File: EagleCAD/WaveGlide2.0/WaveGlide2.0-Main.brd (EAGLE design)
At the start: 80 x 100 mm, 47 parts, among them CN3 0, IC1 MC33502D, K2 MS-20-310-HN, Q2 reset, U1 ATMEGA328P_TQFP, U2 BMP180, U3 MPXV7002, U4 TPS55340PWP, U5 UG-2828GDEDF11, Y2 12MHz

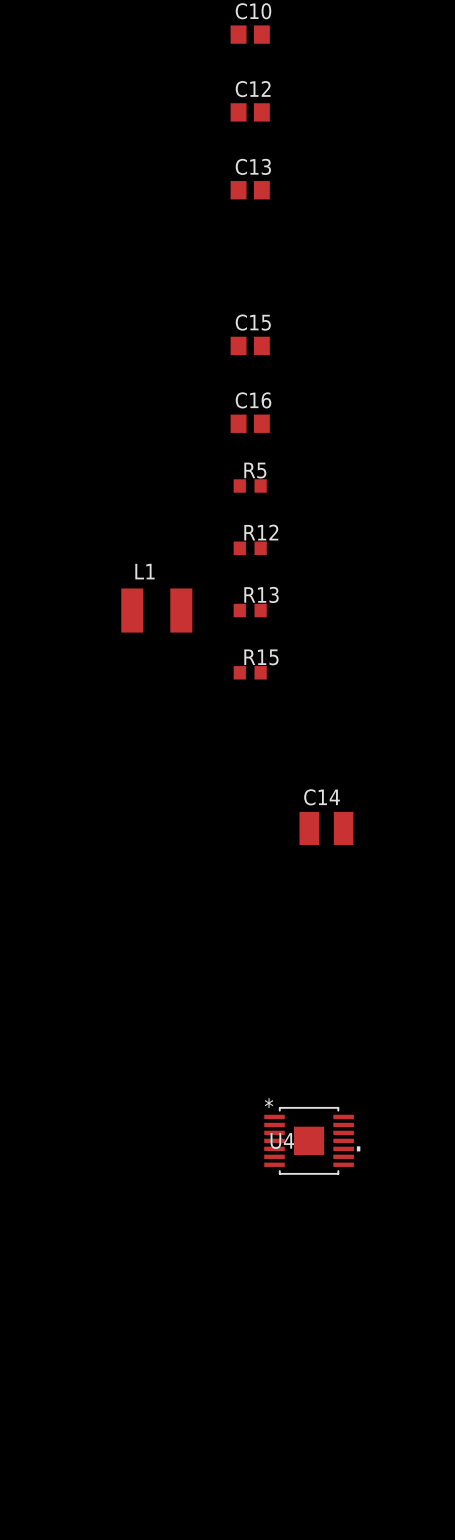
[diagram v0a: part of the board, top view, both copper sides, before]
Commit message: Add 5V regulator
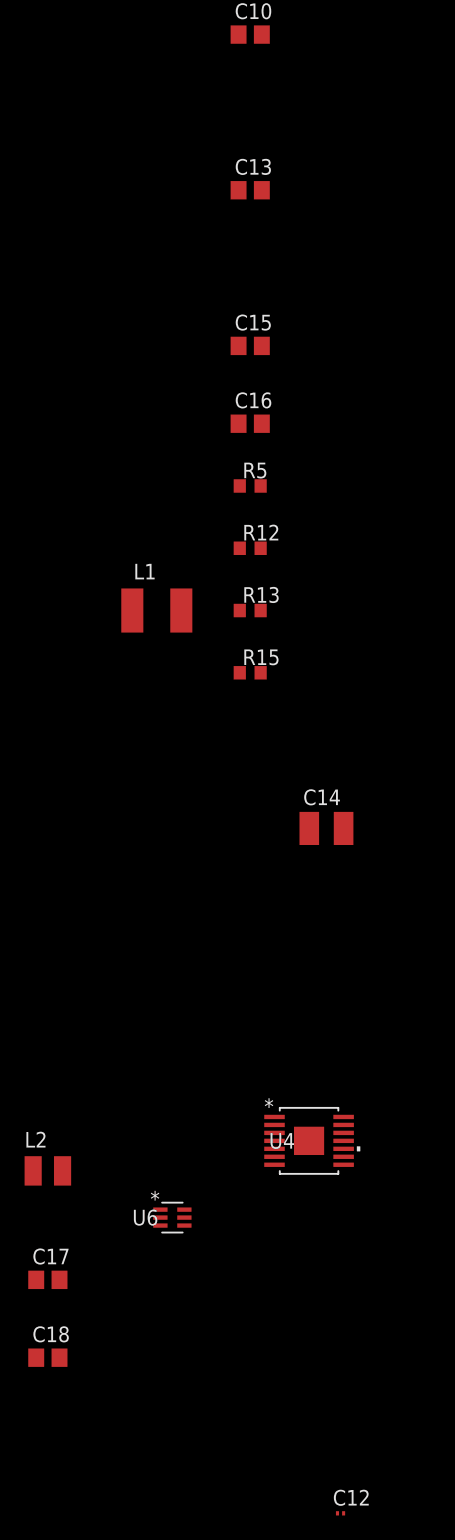
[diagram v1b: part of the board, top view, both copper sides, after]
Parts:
- added C17, C18: 10uF, resistor:C0805
- added L2: 4.7uH, resistor:L2825P
- added U6: TPS61222DCKR, CustomParts:DCK6
- C12: device resistor:C0805 -> resistor:C0201
- moved C12 114.5 mm to (-0.25, -132.1)
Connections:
- new net 5V_EN: U6.6
- new net N$6: L2.2, U6.5
- net GND: now also C17.2, C18.2, U6.3
- net SYS_5V: now also C18.1, U6.2, U6.4
- net TPS55340_SW: now also L1.2; no longer L1.1
- net VBAT: now also C17.1, L1.1, L2.1, U6.1; no longer L1.2

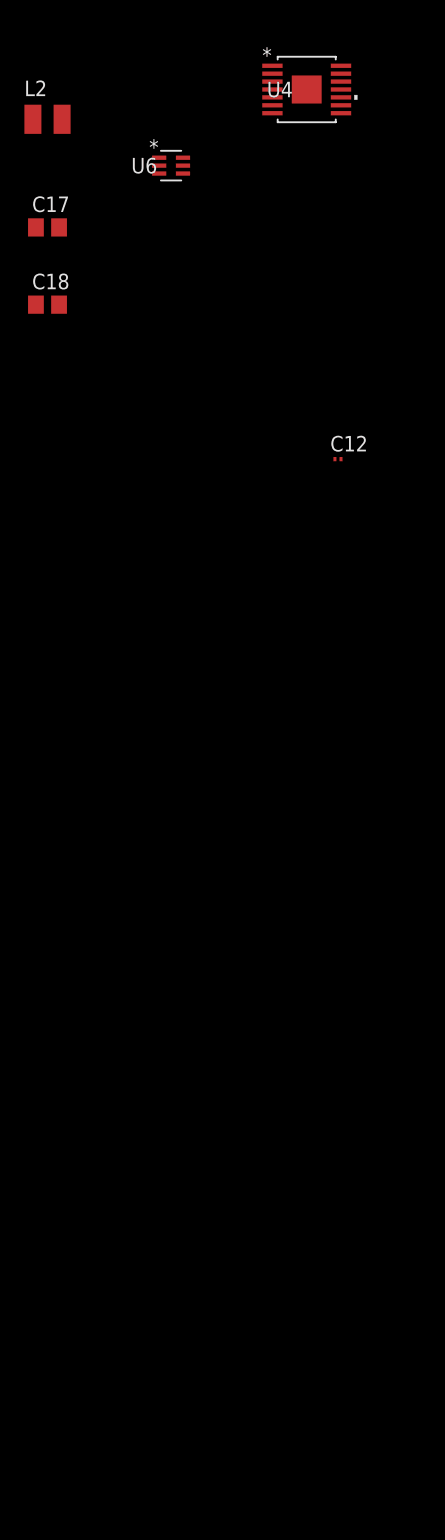
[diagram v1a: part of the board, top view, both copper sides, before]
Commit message: Add 13V boost for OLED
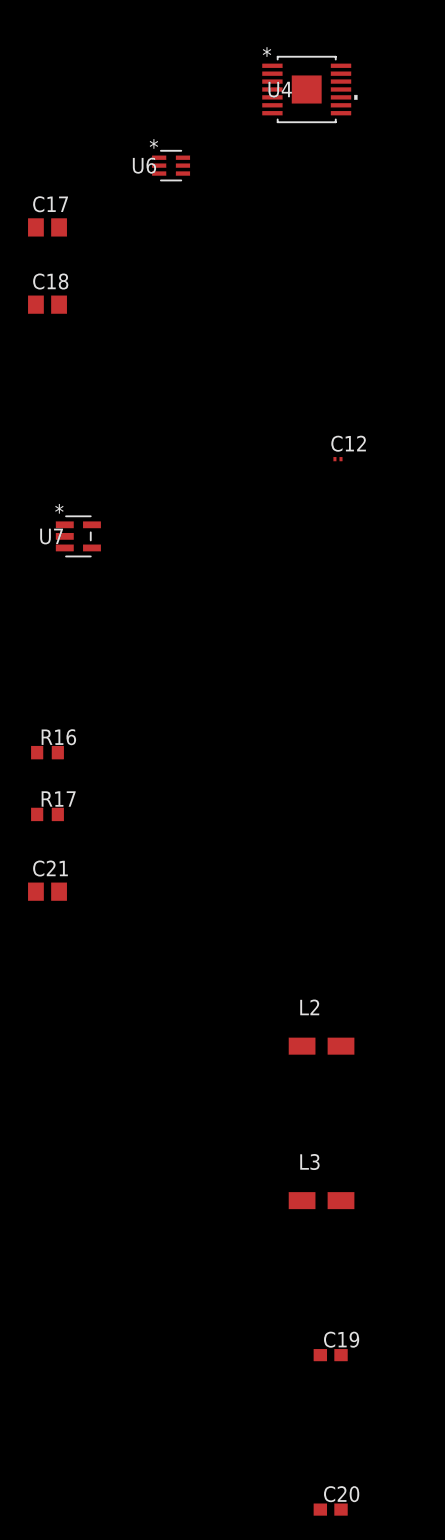
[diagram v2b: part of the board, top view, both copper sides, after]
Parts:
- added C19: 4.7uF, resistor:C0603
- added C20: 47pF, resistor:C0603
- added C21: 1uF, resistor:C0805
- added L3: 18uH, resistor:L4035M
- added R16: 1.5M, resistor:R0603
- added R17: 158k, resistor:R0603
- added U7: TPS61041DBVR, CustomParts:DBV5
- L2: device resistor:L2825P -> resistor:L4035M
- moved L2 79.5 mm to (-1.60, -180.3)
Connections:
- new net 13V_EN: U7.4
- new net N$5: L3.2, U7.1
- new net TPS55340_FB1: C20.2, R16.2, R17.1, U7.3
- net GND: now also C19.2, C21.2, R17.2, U7.2
- net SYS_13V: now also C20.1, C21.1, R16.1
- net VBAT: now also C19.1, L3.1, U7.5
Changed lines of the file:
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@@
 <attribute name="VENDOR" value="Texas Instruments" x="-13.97" y="-107.95" size="1.778" layer="27" display="off"/>
 </element>
-<element name="L2" library="resistor" library_urn="urn:adsk.eagle:library:348" package="L2825P" package3d_urn="urn:adsk.eagle:package:25928/1" value="4.7uH" x="-24.13" y="-104.14">
-<attribute name="MPN" value="LQM2HPN4R7MGCL" x="-24.13" y="-104.14" size="1.778" layer="27" display="off"/>
-<attribute name="POPULATE" value="1" x="-24.13" y="-104.14" size="1.778" layer="27" display="off"/>
+<element name="L2" library="resistor" library_urn="urn:adsk.eagle:library:348" package="L4035M" package3d_urn="urn:adsk.eagle:package:25933/1" value="4.7uH" x="-1.6" y="-180.34">
+<attribute name="MPN" value="LQM2HPN4R7MGCL" x="-1.6" y="-180.34" size="1.778" layer="27" display="off"/>
+<attribute name="POPULATE" value="1" x="-1.6" y="-180.34" size="1.778" layer="27" display="off"/>
 </element>
 <element name="C17" library="resistor" library_urn="urn:adsk.eagle:library:348" package="C0805" package3d_urn="urn:adsk.eagle:package:26137/1" value="10uF" x="-24.13" y="-113.03">
@@
 <attribute name="TOL" value="10%" x="-24.13" y="-119.38" size="1.778" layer="27" display="off"/>
 <attribute name="VOLT" value="10V" x="-24.13" y="-119.38" size="1.778" layer="27" display="off"/>
+</element>
+<element name="U7" library="CustomParts" library_urn="urn:adsk.eagle:library:2193978" package="DBV5" package3d_urn="urn:adsk.eagle:package:2443208/1" value="TPS61041DBVR" x="-21.59" y="-138.43">
+<attribute name="MANUFACTURER_PART_NUMBER" value="TPS61041DBVR" x="-21.59" y="-138.43" size="0.8" layer="27" ratio="14" display="off"/>
+<attribute name="VENDOR" value="Texas Instruments" x="-21.59" y="-138.43" size="0.8" layer="27" ratio="14" display="off"/>
+</element>
+<element name="C19" library="resistor" library_urn="urn:adsk.eagle:library:348" package="C0603" package3d_urn="urn:adsk.eagle:package:26138/1" value="4.7uF" x="-0.85" y="-205.74">
+<attribute name="MPN" value="GRM188R60J475KE19D" x="-0.85" y="-205.74" size="0.8" layer="27" ratio="14" display="off"/>
+<attribute name="POPULATE" value="1" x="-0.85" y="-205.74" size="0.8" layer="27" ratio="14" display="off"/>
+<attribute name="TOL" value="10%" x="-0.85" y="-205.74" size="0.8" layer="27" ratio="14" display="off"/>
+<attribute name="VOLT" value="6.3V" x="-0.85" y="-205.74" size="0.8" layer="27" ratio="14" display="off"/>
+</element>
+<element name="C20" library="resistor" library_urn="urn:adsk.eagle:library:348" package="C0603" package3d_urn="urn:adsk.eagle:package:26138/1" value="47pF" x="-0.85" y="-218.44">
+<attribute name="MPN" value="06035A470KAT2A" x="-0.85" y="-218.44" size="0.8" layer="27" ratio="14" display="off"/>
+<attribute name="POPULATE" value="1" x="-0.85" y="-218.44" size="0.8" layer="27" ratio="14" display="off"/>
+<attribute name="TOL" value="10%" x="-0.85" y="-218.44" size="0.8" layer="27" ratio="14" display="off"/>
+<attribute name="VOLT" value="50V" x="-0.85" y="-218.44" size="0.8" layer="27" ratio="14" display="off"/>
+</element>
+<element name="R16" library="resistor" library_urn="urn:adsk.eagle:library:348" package="R0603" package3d_urn="urn:adsk.eagle:package:26057/1" value="1.5M" x="-24.13" y="-156.21">
+<attribute name="MPN" value="CRCW06031M50FKEA" x="-24.13" y="-156.21" size="0.8" layer="27" ratio="14" display="off"/>
+<attribute name="POPULATE" value="1" x="-24.13" y="-156.21" size="0.8" layer="27" ratio="14" display="off"/>
+<attribute name="TOL" value="1%" x="-24.13" y="-156.21" size="1.778" layer="27" display="off"/>
+</element>
+<element name="R17" library="resistor" library_urn="urn:adsk.eagle:library:348" package="R0603" package3d_urn="urn:adsk.eagle:package:26057/1" value="158k" x="-24.13" y="-161.29">
+<attribute name="MPN" value="CRCW0603158KFKEA" x="-24.13" y="-161.29" size="0.8" layer="27" ratio="14" display="off"/>
+<attribute name="POPULATE" value="1" x="-24.13" y="-161.29" size="0.8" layer="27" ratio="14" display="off"/>
+</element>
+<element name="C21" library="resistor" library_urn="urn:adsk.eagle:library:348" package="C0805" package3d_urn="urn:adsk.eagle:package:26137/1" value="1uF" x="-24.13" y="-167.64">
+<attribute name="MPN" value="GMK212B7105KG" x="-24.13" y="-167.64" size="0.8" layer="27" ratio="14" display="off"/>
+<attribute name="POPULATE" value="1" x="-24.13" y="-167.64" size="0.8" layer="27" ratio="14" display="off"/>
+<attribute name="TOL" value="10%" x="-24.13" y="-167.64" size="0.8" layer="27" ratio="14" display="off"/>
+<attribute name="VOLT" value="35V" x="-24.13" y="-167.64" size="0.8" layer="27" ratio="14" display="off"/>
+</element>
+<element name="L3" library="resistor" library_urn="urn:adsk.eagle:library:348" package="L4035M" package3d_urn="urn:adsk.eagle:package:25933/1" value="18uH" x="-1.6" y="-193.04">
+<attribute name="MPN" value="LPS4018-183MRB" x="-1.6" y="-193.04" size="0.8" layer="27" ratio="14" display="off"/>
+<attribute name="POPULATE" value="1" x="-1.6" y="-193.04" size="0.8" layer="27" ratio="14" display="off"/>
+<attribute name="TOL" value="20%" x="-1.6" y="-193.04" size="1.778" layer="27" display="off"/>
 </element>
 </elements>
@@
 <contactref element="C18" pad="2"/>
 <contactref element="U6" pad="3"/>
+<contactref element="R17" pad="2"/>
+<contactref element="C21" pad="2"/>
+<contactref element="U7" pad="2"/>
+<contactref element="C19" pad="2"/>
+<wire x1="-23.28" y1="-161.29" x2="-23.18" y2="-167.64" width="0" layer="19" extent="1-1"/>
+<wire x1="0" y1="-205.74" x2="-23.28" y2="-161.29" width="0" layer="19" extent="1-1"/>
+<wire x1="-22.7076" y1="-138.43" x2="0" y2="-205.74" width="0" layer="19" extent="1-1"/>
+<wire x1="-23.18" y1="-119.38" x2="-22.7076" y2="-138.43" width="0" layer="19" extent="1-1"/>
 <wire x1="-23.18" y1="-113.03" x2="-23.18" y2="-119.38" width="0" layer="19" extent="1-1"/>
 <wire x1="-14.9479" y1="-108.6" x2="-23.18" y2="-113.03" width="0" layer="19" extent="1-1"/>
@@
 <wire x1="-6.67" y1="-36.83" x2="-6.67" y2="-43.18" width="0" layer="19" extent="1-1"/>
 <wire x1="-6.67" y1="-24.13" x2="-6.67" y2="-36.83" width="0" layer="19" extent="1-1"/>
-<wire x1="0" y1="-132.08" x2="-6.67" y2="-24.13" width="0" layer="19" extent="1-1"/>
-<wire x1="-6.67" y1="-11.43" x2="0" y2="-132.08" width="0" layer="19" extent="1-1"/>
+<wire x1="-6.67" y1="-11.43" x2="-6.67" y2="-24.13" width="0" layer="19" extent="1-1"/>
 <wire x1="-6.67" y1="-5.08" x2="-6.67" y2="-11.43" width="0" layer="19" extent="1-1"/>
+<wire x1="0" y1="-132.08" x2="-22.7076" y2="-138.43" width="0" layer="19" extent="1-1"/>
 <wire x1="35.3" y1="31" x2="-6.67" y2="-5.08" width="0" layer="19" extent="1-1"/>
 <wire x1="40" y1="26.25" x2="35.3" y2="31" width="0" layer="19" extent="1-1"/>
@@
 <contactref element="U5" pad="P$29"/>
 <contactref element="C11" pad="1"/>
-<wire x1="47.498" y1="91.628" x2="46.75" y2="94.088" width="0" layer="19" extent="16-16"/>
+<contactref element="R16" pad="1"/>
+<contactref element="C20" pad="1"/>
+<contactref element="C21" pad="1"/>
+<wire x1="-24.98" y1="-156.21" x2="-25.08" y2="-167.64" width="0" layer="19" extent="1-1"/>
+<wire x1="-1.7" y1="-218.44" x2="-24.98" y2="-156.21" width="0" layer="19" extent="1-1"/>
+<wire x1="47.498" y1="91.628" x2="-1.7" y2="-218.44" width="0" layer="19" extent="1-16"/>
+<wire x1="46.75" y1="94.088" x2="47.498" y2="91.628" width="0" layer="19" extent="16-16"/>
 </signal>
 <signal name="OLED_VSL">
@@
 <contactref element="U6" pad="1"/>
 <contactref element="L2" pad="1"/>
-<wire x1="-25.33" y1="-104.14" x2="-25.08" y2="-113.03" width="0" layer="19" extent="1-1"/>
-<wire x1="-14.9479" y1="-107.3" x2="-25.33" y2="-104.14" width="0" layer="19" extent="1-1"/>
+<contactref element="C19" pad="1"/>
+<contactref element="U7" pad="5"/>
+<contactref element="L3" pad="1"/>
+<wire x1="-3.2" y1="-180.34" x2="-3.2" y2="-193.04" width="0" layer="19" extent="1-1"/>
+<wire x1="-1.7" y1="-205.74" x2="-3.2" y2="-180.34" width="0" layer="19" extent="1-1"/>
+<wire x1="-20.4724" y1="-137.48" x2="-1.7" y2="-205.74" width="0" layer="19" extent="1-1"/>
+<wire x1="-25.08" y1="-113.03" x2="-20.4724" y2="-137.48" width="0" layer="19" extent="1-1"/>
+<wire x1="-14.9479" y1="-107.3" x2="-25.08" y2="-113.03" width="0" layer="19" extent="1-1"/>
 <wire x1="-5.6388" y1="-101.04005625" x2="-14.9479" y2="-107.3" width="0" layer="19" extent="1-1"/>
 <wire x1="-17.24" y1="-58.42" x2="-5.6388" y2="-101.04005625" width="0" layer="19" extent="1-1"/>
@@
 <contactref element="L2" pad="2"/>
 <contactref element="U6" pad="5"/>
-<wire x1="-12.9921" y1="-107.95" x2="-22.93" y2="-104.14" width="0" layer="19" extent="1-1"/>
+<wire x1="-12.9921" y1="-107.95" x2="0" y2="-180.34" width="0" layer="19" extent="1-1"/>
 </signal>
 <signal name="5V_EN">
 <contactref element="U6" pad="6"/>
 </signal>
+<signal name="TPS55340_FB1">
+<contactref element="R16" pad="2"/>
+<contactref element="R17" pad="1"/>
+<contactref element="U7" pad="3"/>
+<contactref element="C20" pad="2"/>
+<wire x1="-23.28" y1="-156.21" x2="-24.98" y2="-161.29" width="0" layer="19" extent="1-1"/>
+<wire x1="0" y1="-218.44" x2="-23.28" y2="-156.21" width="0" layer="19" extent="1-1"/>
+<wire x1="-22.7076" y1="-139.38" x2="0" y2="-218.44" width="0" layer="19" extent="1-1"/>
+</signal>
+<signal name="13V_EN">
+<contactref element="U7" pad="4"/>
+</signal>
+<signal name="N$5">
+<contactref element="L3" pad="2"/>
+<contactref element="U7" pad="1"/>
+<wire x1="-22.7076" y1="-137.48" x2="0" y2="-193.04" width="0" layer="19" extent="1-1"/>
+</signal>
 </signals>

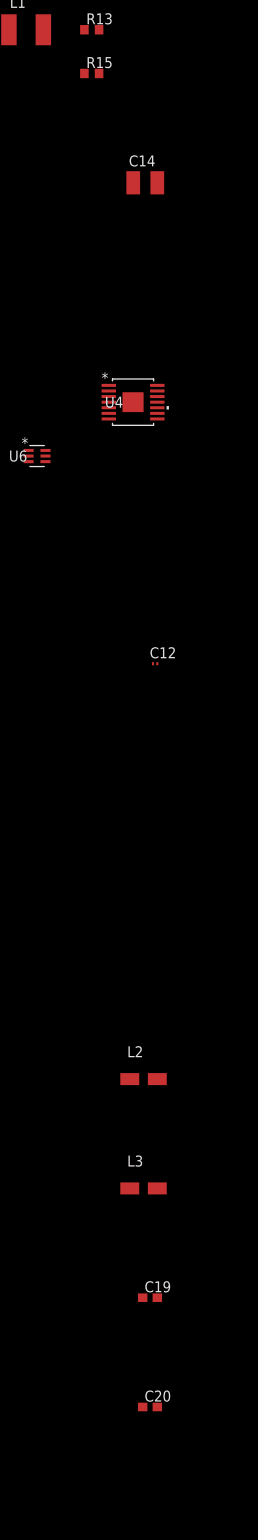
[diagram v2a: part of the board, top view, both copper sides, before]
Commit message: Update BOM fix some bad components
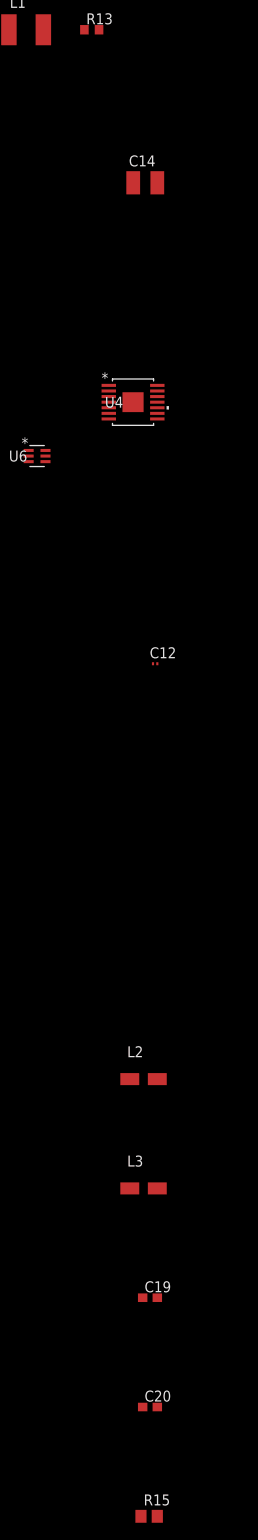
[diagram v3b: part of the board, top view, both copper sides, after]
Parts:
- R15: device resistor:R0603 -> resistor:R0805
- moved R15 167.8 mm to (-0.95, -231.1)
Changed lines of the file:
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@@
 </element>
 <element name="R5" library="resistor" library_urn="urn:adsk.eagle:library:348" package="R0603" package3d_urn="urn:adsk.eagle:package:26057/1" value="60.4k" x="-7.62" y="-48.26">
-<attribute name="MPN" value="CRCW040260K4FKED" x="-7.62" y="-48.26" size="1.778" layer="27" display="off"/>
+<attribute name="MPN" value="CRCW060360K4FKEA" x="-7.62" y="-48.26" size="1.778" layer="27" display="off"/>
 <attribute name="POPULATE" value="1" x="-7.62" y="-48.26" size="1.778" layer="27" display="off"/>
+<attribute name="TOL" value="1%" x="-7.62" y="-48.26" size="1.778" layer="27" display="off"/>
 </element>
 <element name="R12" library="resistor" library_urn="urn:adsk.eagle:library:348" package="R0603" package3d_urn="urn:adsk.eagle:package:26057/1" value="953" x="-7.62" y="-53.34">
-<attribute name="MPN" value="CRCW0402953RFKED" x="-7.62" y="-53.34" size="1.778" layer="27" display="off"/>
+<attribute name="MPN" value="CRCW0603953RFKEA" x="-7.62" y="-53.34" size="1.778" layer="27" display="off"/>
 <attribute name="POPULATE" value="1" x="-7.62" y="-53.34" size="1.778" layer="27" display="off"/>
+<attribute name="TOL" value="1%" x="-7.62" y="-53.34" size="1.778" layer="27" display="off"/>
 </element>
 <element name="R13" library="resistor" library_urn="urn:adsk.eagle:library:348" package="R0603" package3d_urn="urn:adsk.eagle:package:26057/1" value="86.6k" x="-7.62" y="-58.42">
-<attribute name="MPN" value="CRCW040286K6FKED" x="-7.62" y="-58.42" size="1.778" layer="27" display="off"/>
+<attribute name="MPN" value="CRCW060386K6FKEA" x="-7.62" y="-58.42" size="1.778" layer="27" display="off"/>
 <attribute name="POPULATE" value="1" x="-7.62" y="-58.42" size="1.778" layer="27" display="off"/>
-</element>
-<element name="R15" library="resistor" library_urn="urn:adsk.eagle:library:348" package="R0603" package3d_urn="urn:adsk.eagle:package:26057/1" value="10k" x="-7.62" y="-63.5">
-<attribute name="MPN" value="RR1220P-103-D" x="-7.62" y="-63.5" size="1.778" layer="27" display="off"/>
-<attribute name="POPULATE" value="1" x="-7.62" y="-63.5" size="1.778" layer="27" display="off"/>
+<attribute name="TOL" value="1%" x="-7.62" y="-58.42" size="1.778" layer="27" display="off"/>
+</element>
+<element name="R15" library="resistor" library_urn="urn:adsk.eagle:library:348" package="R0805" package3d_urn="urn:adsk.eagle:package:26059/1" value="10k" x="-0.95" y="-231.14">
+<attribute name="MPN" value="RR1220P-103-D" x="-0.95" y="-231.14" size="1.778" layer="27" display="off"/>
+<attribute name="POPULATE" value="1" x="-0.95" y="-231.14" size="1.778" layer="27" display="off"/>
+<attribute name="TOL" value="0.5%" x="-0.95" y="-231.14" size="1.778" layer="27" display="off"/>
 </element>
 <element name="L1" library="resistor" library_urn="urn:adsk.eagle:library:348" package="L4532P" package3d_urn="urn:adsk.eagle:package:25935/1" value="3.3uH" x="-15.24" y="-58.42">
 <attribute name="MPN" value="XAL5030-332MEB" x="-15.24" y="-58.42" size="1.778" layer="27" display="off"/>
 <attribute name="POPULATE" value="1" x="-15.24" y="-58.42" size="1.778" layer="27" display="off"/>
+<attribute name="TOL" value="20%" x="-15.24" y="-58.42" size="1.778" layer="27" display="off"/>
 </element>
 <element name="U4" library="CustomParts" library_urn="urn:adsk.eagle:library:2193978" package="PWP14" package3d_urn="urn:adsk.eagle:package:2335473/3" value="TPS55340PWP" x="-2.8194" y="-101.69006875">
@@
 <wire x1="0" y1="-99.740034375" x2="0" y2="-100.390046875" width="0" layer="19" extent="1-1"/>
 <wire x1="0" y1="-76.2" x2="0" y2="-99.740034375" width="0" layer="19" extent="1-1"/>
-<wire x1="-6.77" y1="-63.5" x2="0" y2="-76.2" width="0" layer="19" extent="1-1"/>
-<wire x1="-8.47" y1="-48.26" x2="-6.77" y2="-63.5" width="0" layer="19" extent="1-1"/>
+<wire x1="0" y1="-231.14" x2="0" y2="-76.2" width="0" layer="19" extent="1-1"/>
+<wire x1="-8.47" y1="-48.26" x2="0" y2="-231.14" width="0" layer="19" extent="1-1"/>
 <wire x1="-6.67" y1="-43.18" x2="-8.47" y2="-48.26" width="0" layer="19" extent="1-1"/>
 <wire x1="-6.67" y1="-36.83" x2="-6.67" y2="-43.18" width="0" layer="19" extent="1-1"/>
@@
 <contactref element="R15" pad="1"/>
 <contactref element="U4" pad="9"/>
-<wire x1="-8.47" y1="-63.5" x2="0" y2="-102.990090625" width="0" layer="19" extent="1-1"/>
-<wire x1="-6.77" y1="-58.42" x2="-8.47" y2="-63.5" width="0" layer="19" extent="1-1"/>
+<wire x1="-1.9" y1="-231.14" x2="0" y2="-102.990090625" width="0" layer="19" extent="1-1"/>
+<wire x1="-6.77" y1="-58.42" x2="-1.9" y2="-231.14" width="0" layer="19" extent="1-1"/>
 </signal>
 <signal name="TPS55340_SW">
